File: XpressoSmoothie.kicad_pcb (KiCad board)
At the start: 2 copper layers, 99.7 x 99.7 mm, 136 parts, among them J1 HEADER_4, J10 HEADER_3X2, J11 Pwr_in, J12 HEADER_4, J13 HEADER_4X2, J14 HEADER_3X2, J15 HEADER_4, J16 HEADER_4, J17 HEADER_4, J172 HEADER_2, J18 HEADER_4, J19 HEADER_2, J2 HEADER_4, J20 HEADER_2, J21 HEADER_2, J22 HEADER_2, J23 HEADER_4, J232 HEADER_2, J24 HEADER_4, J25 HEADER_4, J252 HEADER_2, J26 USB, J27 HEADER_4, J28 MICROSD-MOLEX, J29 HEADER_4, J3 HEADER_3, J4 HEADER_3X2, J5 HEADER_3X2, J6 LPCXPRESSO_GENERIC_HEADER, J7 HEADER_4, J8 HEADER_4, J9 HEADER_3X2, M1 LOGO_OSHW, M2 LOGO_OSHW, Q1 IRLB 8743, Q2 IRLB 8743, Q3 IRLB 8743, Q4 IRLB 8743, SW1 SW_PUSH, SW2 SW_PUSH, SW3 SW_PUSH, U1 POLOLU_A4988, U10 TC4422A, U11 TC4422A, U12 LM1117-3.3, U2 POLOLU_A4988, U3 POLOLU_A4988, U4 POLOLU_A4988, U5 POLOLU_A4988, U7 LM7809CT, U8 TC4422A, U9 TC4422A

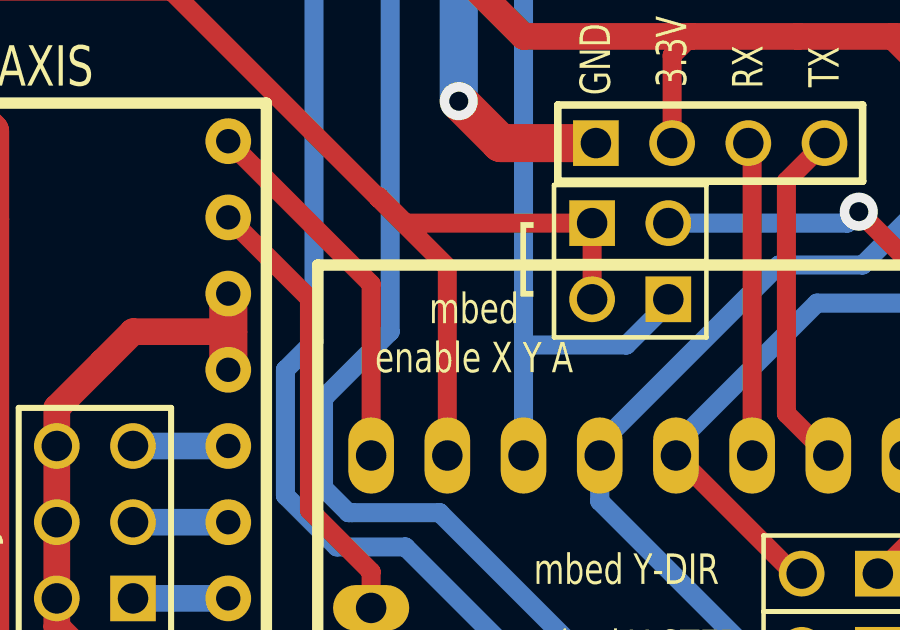
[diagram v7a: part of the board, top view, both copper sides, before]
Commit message: Minor silkscreen changes.
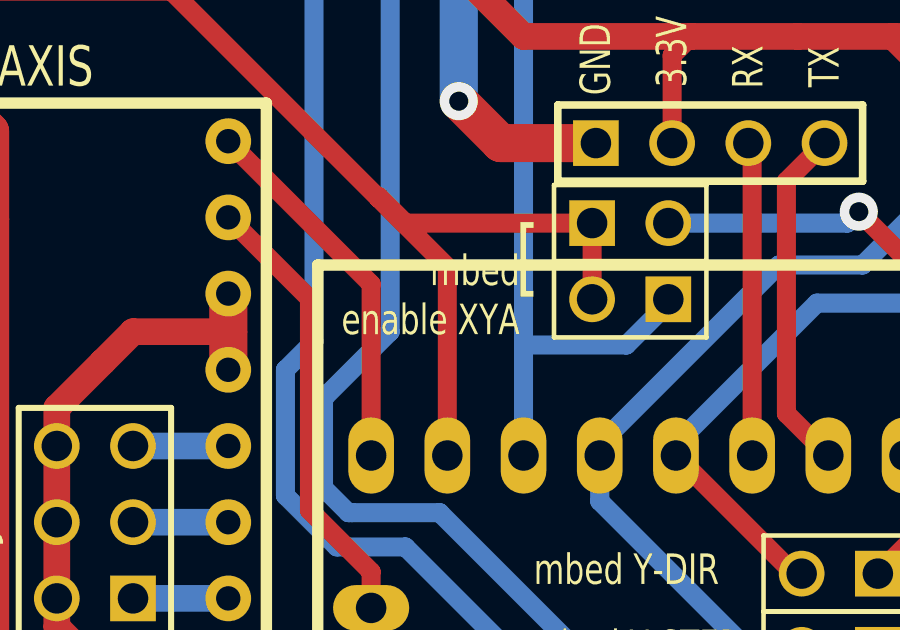
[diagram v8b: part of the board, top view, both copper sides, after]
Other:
- board text added: "mbed enable XYA"
- board text removed: "mbed enable X Y A"
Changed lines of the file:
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@@
     (links 359)
     (no_connects 5)
-    (area 56.388 52.51262 187.467201 163.2712)
+    (area 56.388 52.51262 179.864657 163.2712)
     (thickness 1.6)
     (drawings 45)
@@
     (descr http://www.molex.com/elqNow/elqRedir.htm?ref=http://www.molex.com/pdm_docs/ps/PS-47309-001.pdf)
     (attr smd)
-    (fp_text reference J28 (at 0 3.1 90) (layer B.SilkS)
+    (fp_text reference J28 (at 0 3.1 90) (layer B.SilkS) hide
       (effects (font (size 1.27 1.27) (thickness 0.0889)))
     )
-    (fp_text value MICROSD-MOLEX (at 0 1.3 90) (layer B.SilkS)
+    (fp_text value MICROSD-MOLEX (at 0 1.3 90) (layer B.SilkS) hide
       (effects (font (size 0.7 0.7) (thickness 0.0889)))
     )
@@
     (effects (font (size 1.016 0.762) (thickness 0.1524)))
   )
-  (gr_text "mbed\nenable X Y A" (at 100.584 89.916) (layer F.SilkS)
-    (effects (font (size 1.016 0.762) (thickness 0.1524)))
+  (gr_text "mbed\nenable XYA" (at 102.108 88.646) (layer F.SilkS)
+    (effects (font (size 1.016 0.762) (thickness 0.1524)) (justify right))
   )
   (gr_text "5V from USB" (at 162.179 125.857) (layer F.SilkS)
